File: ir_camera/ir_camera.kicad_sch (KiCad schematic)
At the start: 23 parts, among them J1 PowerIn, J2 Screen, U1 L7805, U2 ATMEGA328P-PU, U3 LD1117, U4 pixart_ir, Y1 Crystal_4pin, Y2 Crystal

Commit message: IR Camera v0.2
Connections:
- net SLC is gone; now on net SCL: U4.5 (SLC)
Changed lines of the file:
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@@
 		)
 	)
-	(global_label "SLC"
+	(global_label "SCL"
 		(shape input)
 		(at 138.43 146.05 180)
@@
 		)
 		(property "Intersheetrefs" "${INTERSHEET_REFS}"
-			(at 130.8526 146.05 0)
+			(at 130.0677 146.05 0)
 			(effects
 				(font

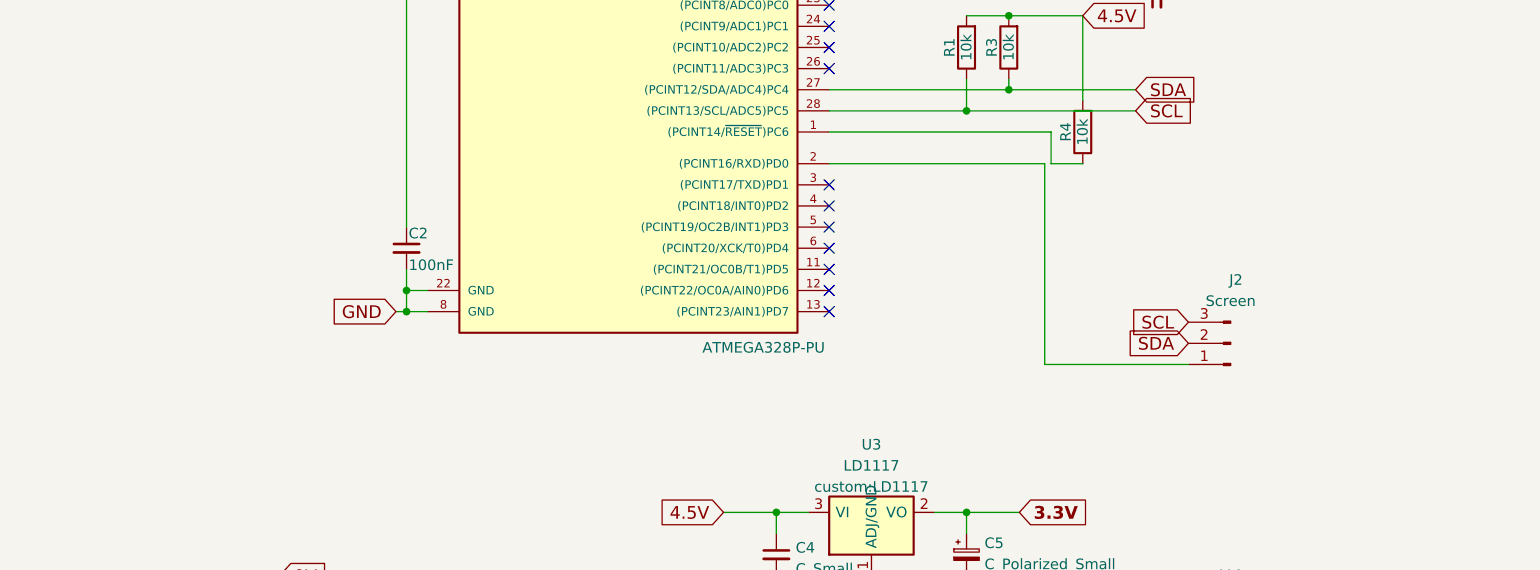
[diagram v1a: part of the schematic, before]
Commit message: IR Camera v0.2: add programming header
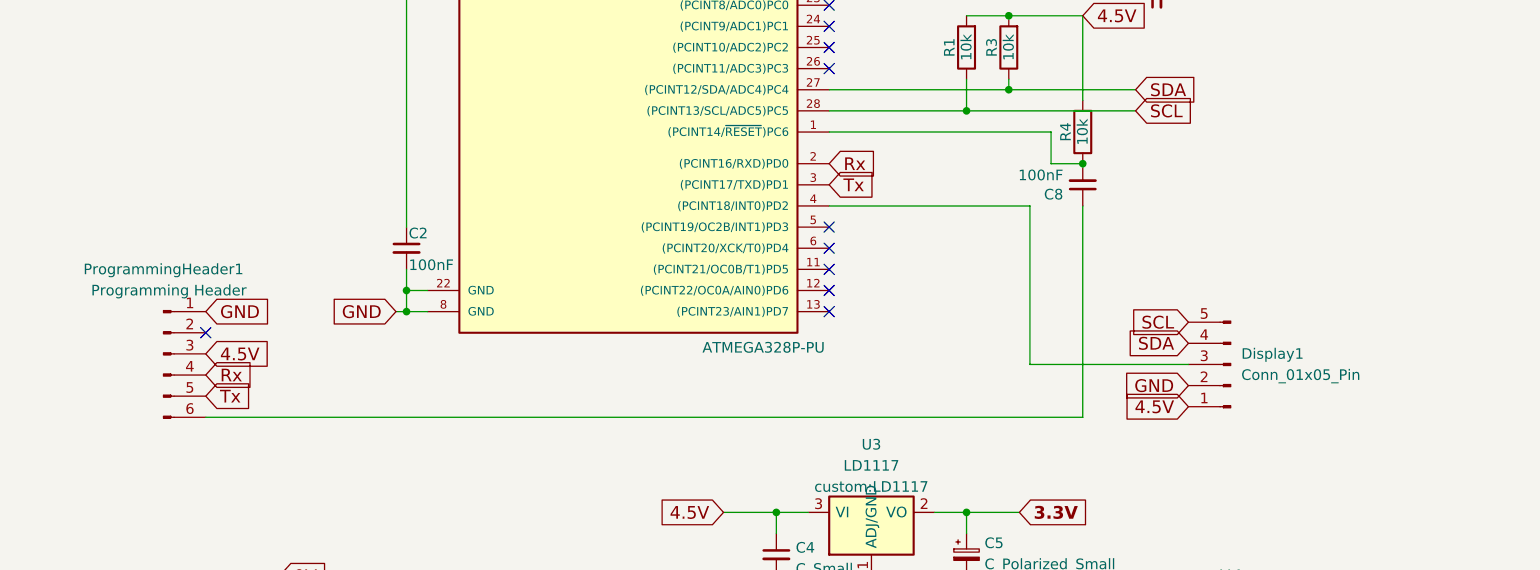
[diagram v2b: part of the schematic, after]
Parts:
- removed J2: Screen, Connector_JST:JST_EH_B3B-EH-A_1x03_P2.50mm_Vertical, symbol custom:Conn_01x03_Male
- added C8: 100nF, Capacitor_THT:C_Disc_D5.0mm_W2.5mm_P2.50mm, symbol Device:C_Small
- added Display1: Conn_01x05_Pin, Connector_JST:JST_EH_B5B-EH-A_1x05_P2.50mm_Vertical, symbol Connector:Conn_01x05_Pin
- added ProgrammingHeader1: Programming Header, Connector_PinHeader_2.54mm:PinHeader_1x06_P2.54mm_Horizontal, symbol Connector:Conn_01x06_Pin
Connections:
- net 4.5V: now also Display1.1 (Pin_1), ProgrammingHeader1.3 (Pin_3)
- net GND: now also Display1.2 (Pin_2), ProgrammingHeader1.1 (Pin_1)
- net SCL: now also Display1.5 (Pin_5)
- net SDA: now also Display1.4 (Pin_4)
- net Rx: now reaches U2.2 ((PCINT16/RXD)PD0)
- net Rx: now also ProgrammingHeader1.4 (Pin_4)
- net at R4.1, U2.1 ((PCINT14/~{RESET})PC6): now also C8.2
- net Tx: now reaches U2.3 ((PCINT17/TXD)PD1)
- net Tx: now also ProgrammingHeader1.5 (Pin_5)
- net at U2.4 ((PCINT18/INT0)PD2): now also Display1.3 (Pin_3)
- new net: C8.1, ProgrammingHeader1.6 (Pin_6)
- no-connect marks 20 -> 19
